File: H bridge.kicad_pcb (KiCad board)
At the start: 2 copper layers, 97 x 50 mm, 44 parts, among them J1 Fan, J2 5v Output, J3 Motor Terminal, J4 24v Power Input, J5 Control, Q1 IRLZ44N, Q2 IRLZ44N, Q3 IRLZ44N, Q4 IRLZ44N, SW1 SW_SPST, U1 IR2110, U2 IR2110, U3 LM7815_TO220, U4 LM7805_TO220

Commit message: this is v2.0 it has the IC IR2110. (not tested yet).
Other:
- board text added: "CW: H->PWM L->LOW --------------------- CCW: H->LOW L->PWM --------------------- Stop: H->LOW L->LOW --------------------- Never:H->HIGH L->HIGH"
- board text removed: "CW: H->HIGH L->LOW --------------------- CCW: H->LOW L->HIGH --------------------- Stop: H->LOW L->LOW --------------------- Never:H->HIGH L->HIGH"

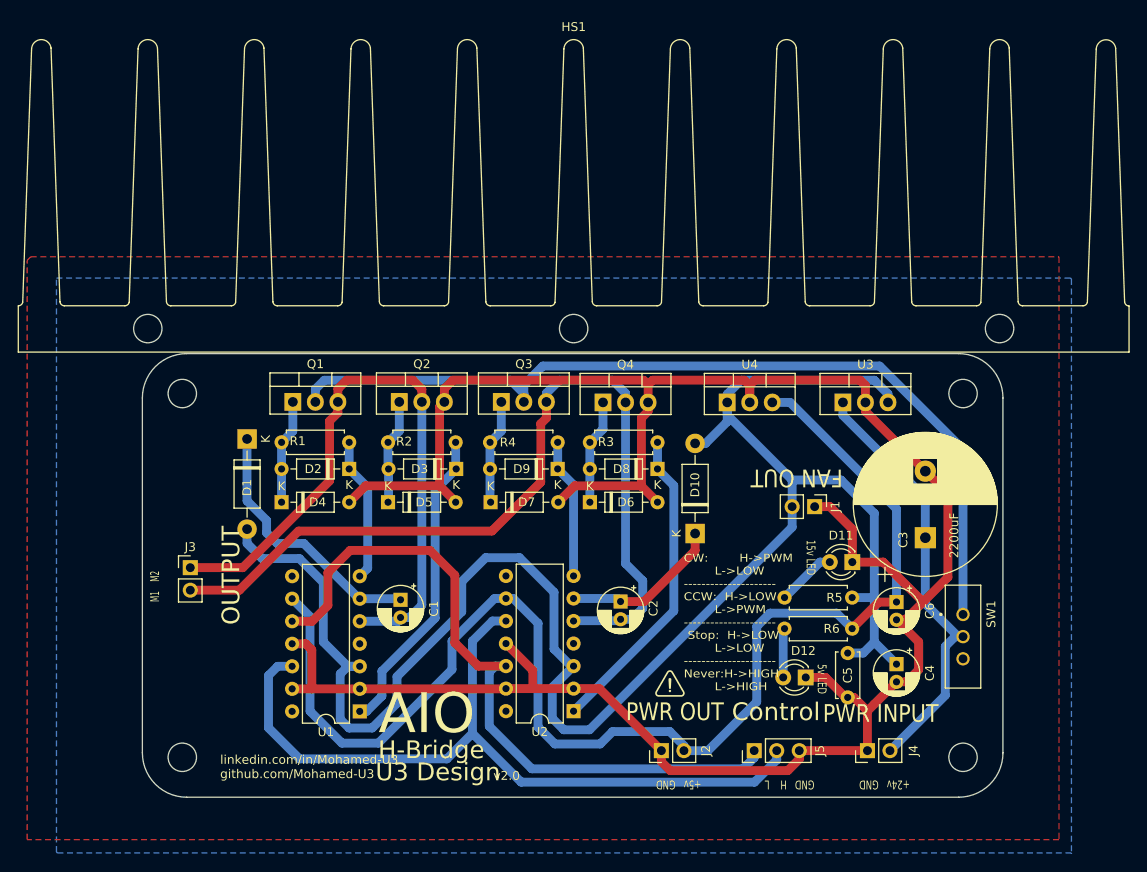
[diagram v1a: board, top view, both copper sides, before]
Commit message: the same thing just adding Atmega328p to give a PWM for the IR2110.
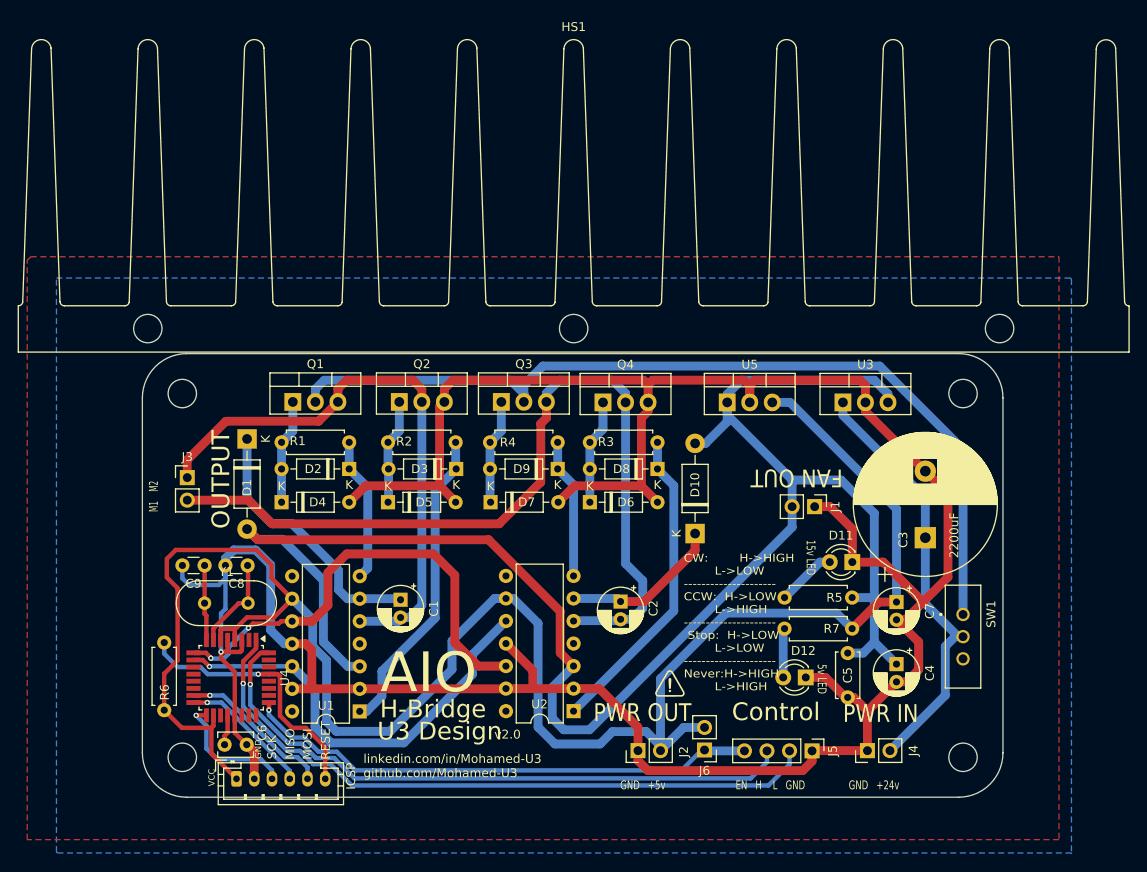
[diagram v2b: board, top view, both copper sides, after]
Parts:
- added C6: 100nF, Capacitor_THT:C_Disc_D3.8mm_W2.6mm_P2.50mm, F.Cu at (125.9, 103.6)
- added C8: 22pF, Capacitor_THT:C_Disc_D3.0mm_W1.6mm_P2.50mm, F.Cu at (126.0, 83.4)
- added C9: 22pF, Capacitor_THT:C_Disc_D3.0mm_W1.6mm_P2.50mm, F.Cu at (121.2, 83.4)
- added J6: 5v Output, Connector_PinHeader_2.54mm:PinHeader_1x02_P2.54mm_Vertical, F.Cu at (177.5, 104.2)
- added J7: ICSP, Connector_JST:JST_PH_B6B-PH-K_1x06_P2.00mm_Vertical, F.Cu at (124.8, 107.5)
- added R6: 10k, Resistor_THT:R_Axial_DIN0207_L6.3mm_D2.5mm_P7.62mm_Horizontal, F.Cu at (116.6, 99.7)
- added U4: ATmega328P-A, Package_QFP:TQFP-32_7x7mm_P0.8mm, F.Cu at (124.2, 96.0)
- added Y1: 16MHz, Crystal:Crystal_HC18-U_Vertical, F.Cu at (121.2, 87.7)
- J5: footprint Connector_PinHeader_2.54mm:PinHeader_1x03_P2.54mm_Vertical -> Connector_PinHeader_2.54mm:PinHeader_1x04_P2.54mm_Vertical
- moved J3 10.2 mm to (119.2, 73.5)
- moved J5 6.52 mm to (189.6, 104.3), turned to -90 degrees
- moved J2 2.64 mm to (170.0, 104.3)
- renumbered C6 to C7, R6 to R7, U4 to U5
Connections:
- J5 pad 1: HIN -> GND
- J5 pad 2: LIN -> 3
- J5 pad 3: GND -> 2
- U1 pad 10: HIN -> 5
- U1 pad 12: LIN -> 6
- U2 pad 10: LIN -> 6
- U2 pad 12: HIN -> 5
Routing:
- net LIN: track 88.4 -> 0.00 mm
- net HIN: track 80.8 -> 0.00 mm
- net 3: track 0.00 -> 75.9 mm, vias 0 -> 1
- net 2: track 0.00 -> 71.0 mm, vias 0 -> 1
- net +5V: track 148.0 -> 214.6 mm
- net A2: track 0.00 -> 58.9 mm, vias 0 -> 1
- net GND: track 265.6 -> 324.4 mm, vias 0 -> 1
- net 5: track 0.00 -> 52.8 mm, vias 0 -> 2
- net 6: track 0.00 -> 48.6 mm, vias 0 -> 1
- net RESET: track 0.00 -> 29.9 mm, vias 0 -> 1
- net 11/MOSI: track 0.00 -> 17.5 mm, vias 0 -> 1
- net 12/MISO: track 0.00 -> 14.9 mm, vias 0 -> 1
- net 13/SCK: track 0.00 -> 14.8 mm, vias 0 -> 1
- net XTAL1: track 0.00 -> 10.7 mm
- net +15V: track 202.8 -> 193.3 mm
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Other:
- board text added: "CW: H->HIGH L->LOW --------------------- CCW: H->LOW L->HIGH --------------------- Stop: H->LOW L->LOW --------------------- Never:H->HIGH L->HIGH"
- board text added: "EN H L GND"
- board text added: "GND"
- board text added: "GND +24v"
- board text added: "GND +5v"
- board text added: "MISO"
- board text added: "MOSI"
- board text added: "PWR IN"
- board text added: "RESET"
- board text added: "SCK"
- board text added: "VCC"
- board text removed: "+24v GND"
- board text removed: "+5v GND"
- board text removed: "CW: H->PWM L->LOW --------------------- CCW: H->LOW L->PWM --------------------- Stop: H->LOW L->LOW --------------------- Never:H->HIGH L->HIGH"
- board text removed: "GND H L"
- board text removed: "PWR INPUT"

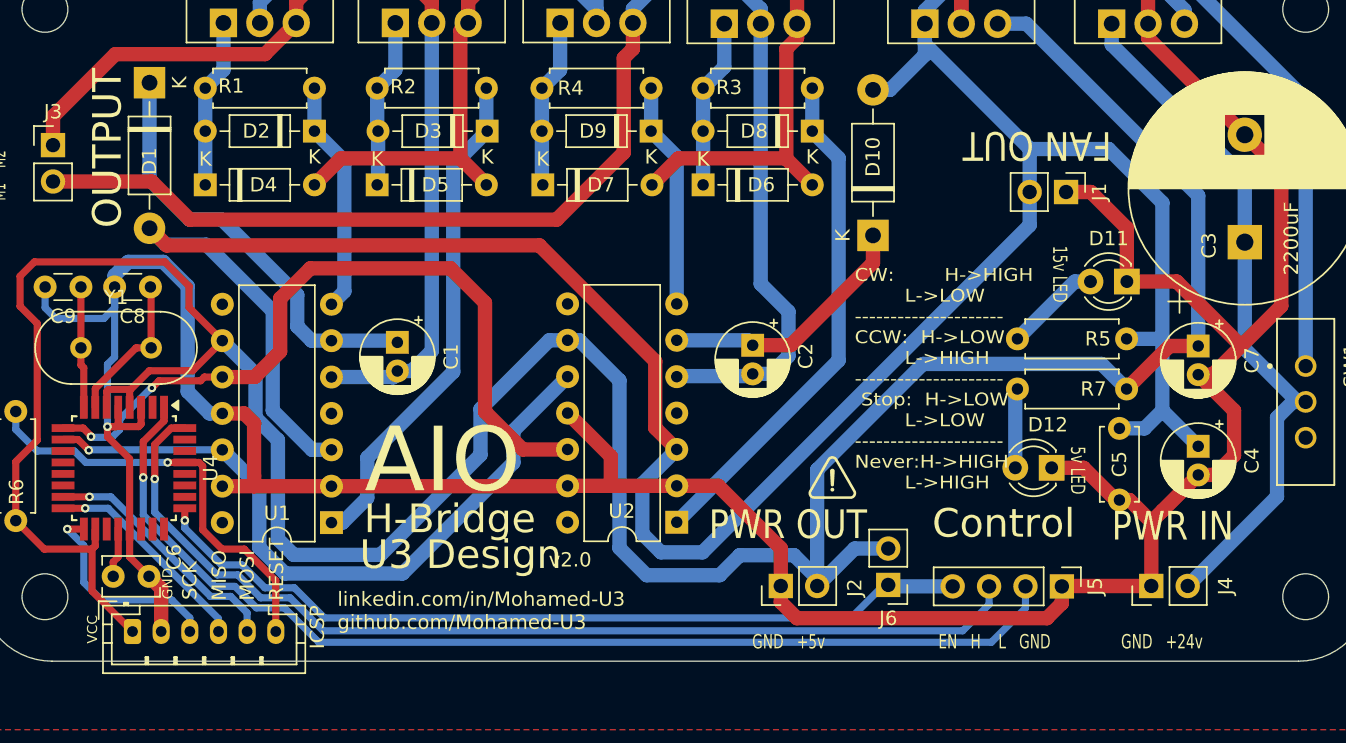
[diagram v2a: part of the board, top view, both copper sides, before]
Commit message: version 2.1 with MCU Atmega328p that uses En and D pins for control only.
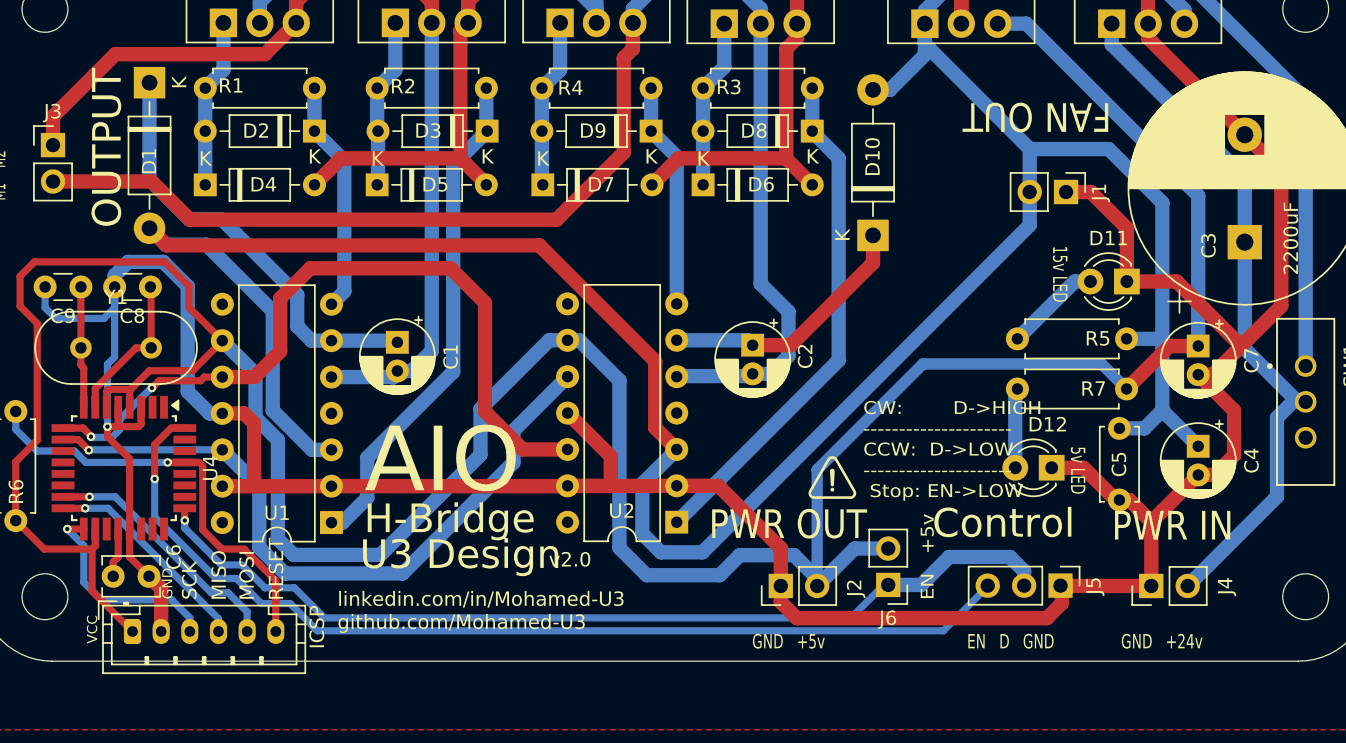
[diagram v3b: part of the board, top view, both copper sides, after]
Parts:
- J5: footprint Connector_PinHeader_2.54mm:PinHeader_1x04_P2.54mm_Vertical -> Connector_PinHeader_2.54mm:PinHeader_1x03_P2.54mm_Vertical
- moved J5 0.11 mm to (189.5, 104.2)
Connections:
- J5 pad 2: 3 -> A2
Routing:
- net 3: track 75.9 -> 0.00 mm, vias 1 -> 0
- net A2: track 58.9 -> 65.8 mm
- net 2: track 71.0 -> 70.5 mm
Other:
- board text added: "CW: D->HIGH --------------------- CCW: D->LOW --------------------- Stop: EN->LOW"
- board text added: "EN +5v"
- board text added: "EN D GND"
- board text removed: "CW: H->HIGH L->LOW --------------------- CCW: H->LOW L->HIGH --------------------- Stop: H->LOW L->LOW --------------------- Never:H->HIGH L->HIGH"
- board text removed: "EN H L GND"
